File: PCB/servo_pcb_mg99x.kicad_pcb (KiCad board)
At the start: 2 copper layers, 35 x 16 mm, 42 parts, among them J1 power in, M1 M1, M2 M2, U1 MM32G0001, U2 SL7533-3, U3 BDR6121H, U4 INA180A2, U5 AS5600

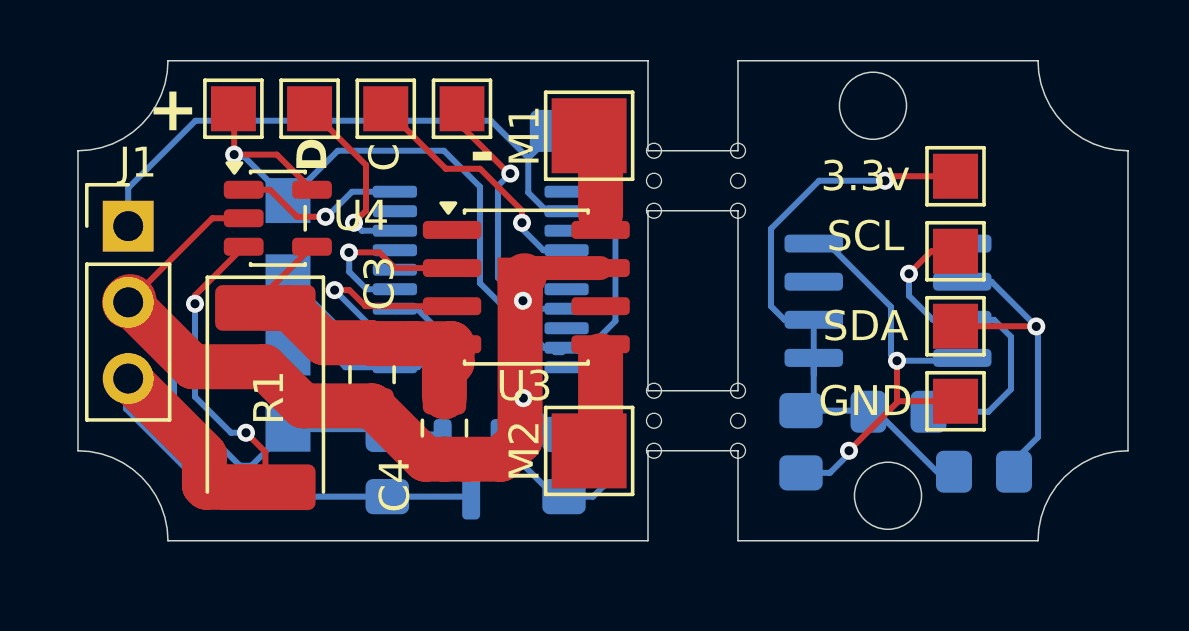
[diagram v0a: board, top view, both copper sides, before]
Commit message: updated pcb:added ground pours
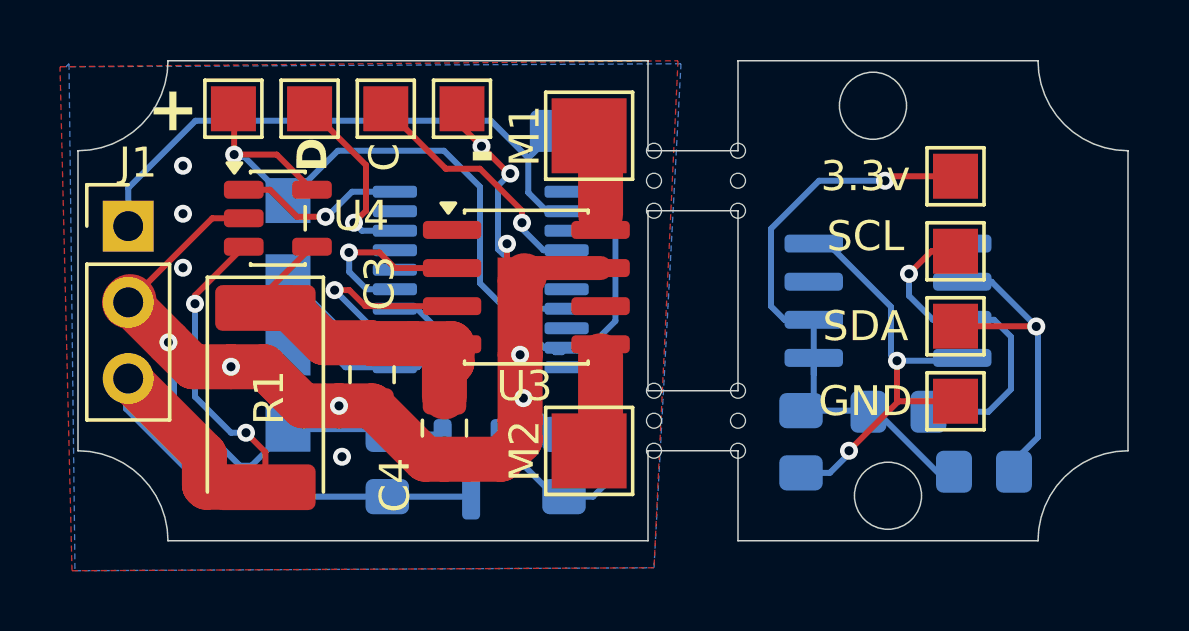
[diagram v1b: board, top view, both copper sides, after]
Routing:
- net GND: track 55.8 -> 56.4 mm, vias 3 -> 12
- added copper zone on B.Cu, net GND
- added copper zone on F.Cu, net GND
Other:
- board text added: "μDrive_1.0"
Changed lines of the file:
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@@
 		)
 		(fp_text user "${REFERENCE}"
-			(at 8.2 -14.17175 90)
+			(at 0 -0.1 90)
 			(layer "B.Fab")
 			(effects
@@
 		)
 		(property "Value" "10K"
-			(at 11 -3.65 0)
+			(at 0 -0.1 0)
 			(layer "B.Fab")
 			(effects
@@
 	)
 	(gr_text ".\n"
-		(at 58.694 42.504 0)
+		(at 69.7 40.9 0)
 		(layer "B.SilkS")
 		(effects
@@
 		)
 	)
+	(gr_text "μDrive_1.0\n"
+		(at 75.5 33.6 0)
+		(layer "B.SilkS")
+		(effects
+			(font
+				(size 1.5 1.5)
+				(thickness 0.2)
+			)
+			(justify left bottom mirror)
+		)
+	)
 	(segment
 		(start 73.34 44.0815)
@@
 	)
 	(segment
-		(start 75.231515 38.799485)
-		(end 75.497752 38.533248)
-		(width 0.8)
-		(layer "F.Cu")
-		(net 2)
-	)
-	(segment
-		(start 75.497752 38.533248)
-		(end 75.497752 38.179752)
-		(width 0.8)
+		(start 74.7 37.382)
+		(end 75.282 37.964)
+		(width 0.2)
 		(layer "F.Cu")
 		(net 2)
@@
 	(segment
 		(start 75.137 42.79)
-		(end 75.137 38.109)
+		(end 75.137 40.6)
 		(width 1.5)
 		(layer "F.Cu")
@@
 	)
 	(segment
+		(start 73.85 33.65)
+		(end 74.8 34.6)
+		(width 0.2)
+		(layer "F.Cu")
+		(net 2)
+	)
+	(segment
 		(start 62.074 38.853)
 		(end 62.080999 38.853)
@@
 	(segment
 		(start 67.9035 42.3035)
-		(end 70.202 42.3035)
+		(end 69.1 42.3035)
 		(width 1.5)
 		(layer "F.Cu")
@@
 	(segment
 		(start 64.227999 41)
-		(end 66.6 41)
+		(end 65.5 41)
 		(width 1.5)
 		(layer "F.Cu")
@@
 	)
 	(segment
-		(start 75.497752 38.179752)
-		(end 75.282 37.964)
-		(width 0.8)
+		(start 63.413999 40.186001)
+		(end 64.227999 41)
+		(width 1.5)
+		(layer "F.Cu")
+		(net 2)
+	)
+	(segment
+		(start 69.1 42.3035)
+		(end 70.202 42.3035)
+		(width 1.5)
 		(layer "F.Cu")
 		(net 2)
@@
 	(segment
 		(start 73.2 33)
-		(end 74.8 34.6)
+		(end 73.85 33.65)
 		(width 0.2)
 		(layer "F.Cu")
@@
 	)
 	(segment
+		(start 75.137 40.6)
+		(end 75.137 38.109)
+		(width 1.5)
+		(layer "F.Cu")
+		(net 2)
+	)
+	(segment
+		(start 74.7 36.9)
+		(end 74.7 37.382)
+		(width 0.2)
+		(layer "F.Cu")
+		(net 2)
+	)
+	(segment
 		(start 62.080999 38.853)
-		(end 64.227999 41)
+		(end 63.413999 40.186001)
 		(width 1.5)
 		(layer "F.Cu")
@@
 	)
 	(segment
+		(start 65.5 41)
+		(end 66.6 41)
+		(width 1.5)
+		(layer "F.Cu")
+		(net 2)
+	)
+	(segment
 		(start 74.8 34.6)
 		(end 74.809 34.591)
@@
 	)
 	(via
-		(at 75.231515 38.799485)
+		(at 69.2 44)
+		(size 0.6)
+		(drill 0.3)
+		(layers "F.Cu" "B.Cu")
+		(free yes)
+		(net 2)
+	)
+	(via
+		(at 69.1 42.3035)
+		(size 0.6)
+		(drill 0.3)
+		(layers "F.Cu" "B.Cu")
+		(net 2)
+	)
+	(via
+		(at 63.9 34.3)
+		(size 0.6)
+		(drill 0.3)
+		(layers "F.Cu" "B.Cu")
+		(free yes)
+		(net 2)
+	)
+	(via
+		(at 63.9 37.7)
 		(size 0.6)
 		(drill 0.3)
 		(layers "F.Cu" "B.Cu")
+		(free yes)
 		(net 2)
 	)
@@
 	)
 	(via
+		(at 65.5 41)
+		(size 0.6)
+		(drill 0.3)
+		(layers "F.Cu" "B.Cu")
+		(net 2)
+	)
+	(via
+		(at 74.7 36.9)
+		(size 0.6)
+		(drill 0.3)
+		(layers "F.Cu" "B.Cu")
+		(net 2)
+	)
+	(via
 		(at 75.245722 42.045722)
 		(size 0.6)
@@
 		(net 2)
 	)
+	(via
+		(at 73.85 33.65)
+		(size 0.6)
+		(drill 0.3)
+		(layers "F.Cu" "B.Cu")
+		(net 2)
+	)
+	(via
+		(at 75.137 40.6)
+		(size 0.6)
+		(drill 0.3)
+		(layers "F.Cu" "B.Cu")
+		(net 2)
+	)
+	(via
+		(at 63.9 35.9)
+		(size 0.6)
+		(drill 0.3)
+		(layers "F.Cu" "B.Cu")
+		(free yes)
+		(net 2)
+	)
+	(via
+		(at 63.413999 40.186001)
+		(size 0.6)
+		(drill 0.3)
+		(layers "F.Cu" "B.Cu")
+		(net 2)
+	)
 	(segment
 		(start 75.245722 42.045722)
@@
 	)
 	(segment
-		(start 75.231515 38.799485)
-		(end 75.49803 39.066)
+		(start 74.4 37.082)
+		(end 74.518 37.082)
 		(width 0.2)
 		(layer "B.Cu")
@@
 	)
 	(segment
-		(start 74.4 38.032)
-		(end 74.4 34.969472)
+		(start 63.6 42.1)
+		(end 63.6 40.379)
 		(width 0.2)
 		(layer "B.Cu")
@@
 	)
 	(segment
-		(start 63.6 42.1)
-		(end 63.6 40.379)
+		(start 75.282 37.964)
+		(end 74.4 37.082)
 		(width 0.2)
 		(layer "B.Cu")
@@
 	)
 	(segment
+		(start 75.282 37.964)
+		(end 75.282 38.84997)
+		(width 0.2)
+		(layer "B.Cu")
+		(net 2)
+	)
+	(segment
 		(start 72.327 43.255)
 		(end 72.554 43.482)
@@
 	)
 	(segment
-		(start 67.4 43.08)
-		(end 66.18 44.3)
+		(start 75.282 38.84997)
+		(end 75.49803 39.066)
 		(width 0.2)
 		(layer "B.Cu")
@@
 	)
 	(segment
-		(start 75.167485 38.799485)
-		(end 74.4 38.032)
+		(start 67.4 43.08)
+		(end 66.18 44.3)
 		(width 0.2)
 		(layer "B.Cu")
@@
 	)
 	(segment
-		(start 76.455 43.255)
-		(end 76.6 43.255)
+		(start 74.4 37.082)
+		(end 74.4 34.969472)
 		(width 0.2)
 		(layer "B.Cu")
@@
 	)
 	(segment
-		(start 70.535 43.08)
-		(end 70.71 43.255)
+		(start 74.4 34.969472)
+		(end 74.809 34.560472)
 		(width 0.2)
 		(layer "B.Cu")
@@
 	)
 	(segment
-		(start 75.231515 38.799485)
-		(end 75.167485 38.799485)
+		(start 76.455 43.255)
+		(end 76.6 43.255)
 		(width 0.2)
 		(layer "B.Cu")
@@
 	)
 	(segment
-		(start 74.4 34.969472)
-		(end 74.809 34.560472)
+		(start 70.535 43.08)
+		(end 70.71 43.255)
 		(width 0.2)
 		(layer "B.Cu")
@@
 	)
 	(segment
+		(start 74.518 37.082)
+		(end 74.7 36.9)
+		(width 0.2)
+		(layer "B.Cu")
+		(net 2)
+	)
+	(segment
 		(start 65.605044 32.425044)
 		(end 65.58 32.4)
@@
 		(net 30)
 	)
+	(zone
+		(net 2)
+		(net_name "GND")
+		(layer "F.Cu")
+		(hatch edge 0.5)
+		(connect_pads
+			(clearance 0.5)
+		)
+		(min_thickness 0.25)
+		(filled_areas_thickness no)
+		(fill yes
+			(thermal_gap 0.5)
+			(thermal_bridge_width 0.5)
+		)
+		(polygon
+			(pts
+				(xy 59.8 31) (xy 80.4 30.8) (xy 79.6 47.7) (xy 60.2 47.8)
+			)
+		)
+	)
+	(zone
+		(net 2)
+		(net_name "GND")
+		(layer "B.Cu")
+		(hatch edge 0.5)
+		(priority 1)
+		(connect_pads
+			(clearance 0.5)
+		)
+		(min_thickness 0.25)
+		(filled_areas_thickness no)
+		(fill yes
+			(thermal_gap 0.5)
+			(thermal_bridge_width 0.5)
+		)
+		(polygon
+			(pts
+				(xy 60.1 30.9) (xy 60.3 47.8) (xy 79.6 47.7) (xy 80.5 30.9) (xy 60 31)
+			)
+		)
+	)
 	(group ""

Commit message: updated  the pcb for generic motors
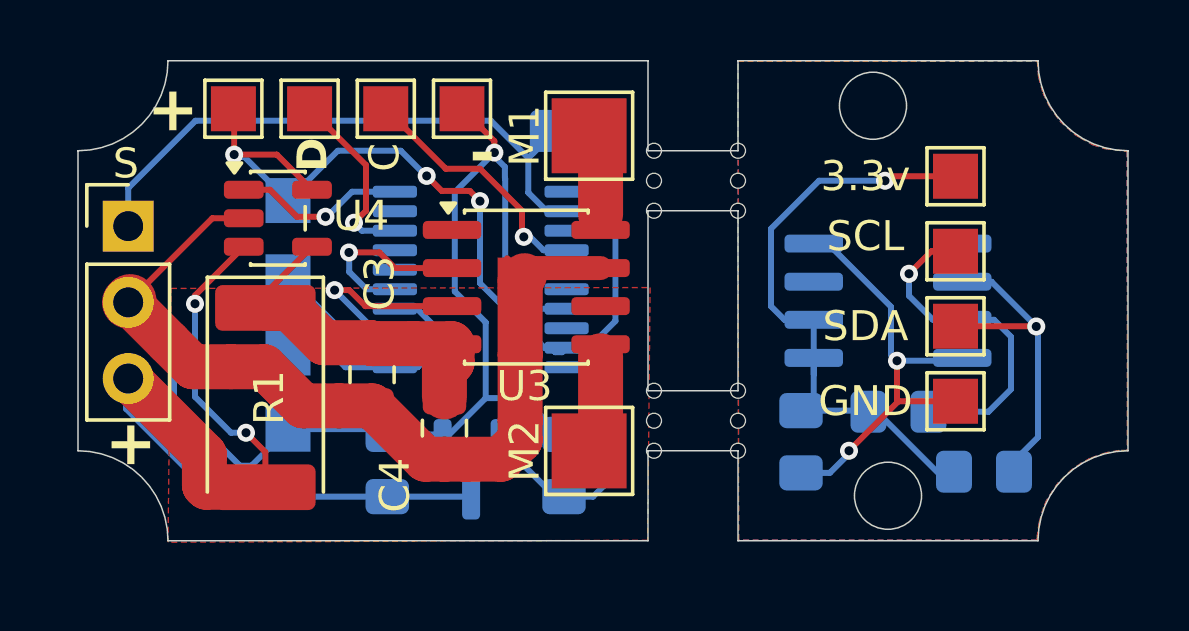
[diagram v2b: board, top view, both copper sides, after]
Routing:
- net GND: track 56.4 -> 68.1 mm, vias 12 -> 1
- net +3.3V: track 40.8 -> 40.5 mm, vias 1 -> 3
- added copper zone on B.Cu, net (none)
- added copper zone on F.Cu, net (none)
- removed copper zone on B.Cu, net GND
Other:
- board text added: "S"

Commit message: fix:update pcb footprint error ,cleanup micropython code
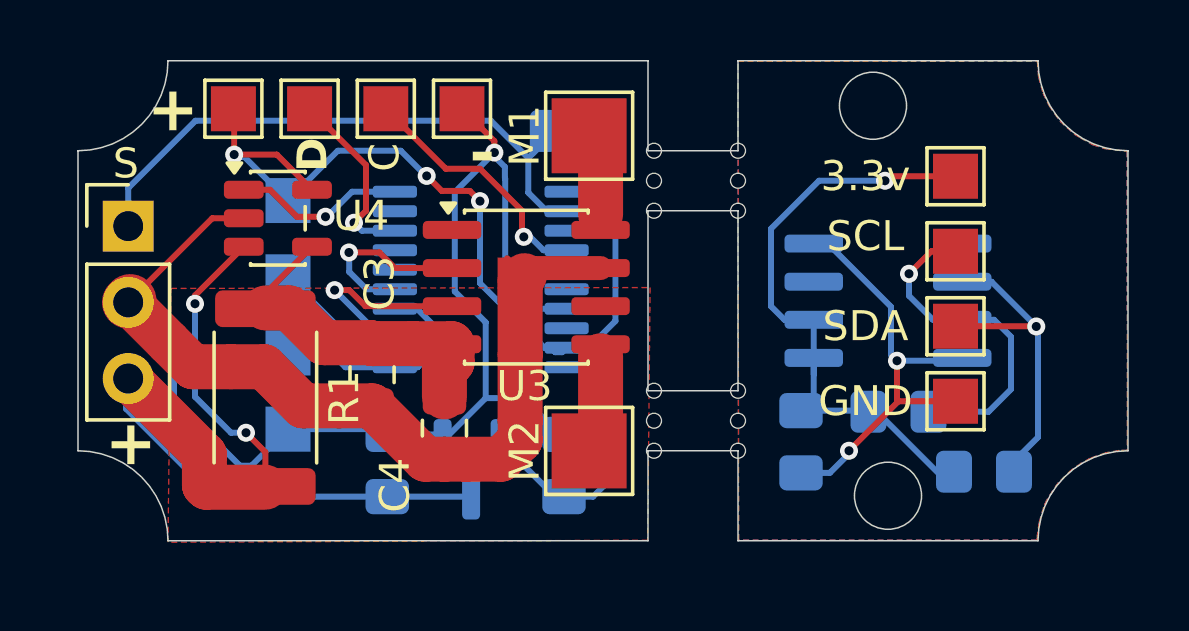
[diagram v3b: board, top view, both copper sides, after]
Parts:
- R1: footprint Diode_SMD:D_2512_6332Metric_Pad1.52x3.35mm_HandSolder -> Resistor_SMD:R_2512_6332Metric
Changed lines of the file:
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@@
 		(embedded_fonts no)
 	)
-	(footprint "Diode_SMD:D_2512_6332Metric_Pad1.52x3.35mm_HandSolder"
+	(footprint "Resistor_SMD:R_2512_6332Metric"
 		(layer "F.Cu")
 		(at 66.646 42.028 -90)
-		(descr "Diode SMD 2512 (6332 Metric), square (rectangular) end terminal, IPC-7351 nominal, (Body size source: http://www.tortai-tech.com/upload/download/2011102023233369053.pdf), generated with kicad-footprint-generator")
-		(tags "diode handsolder")
+		(descr "Resistor SMD 2512 (6332 Metric), square (rectangular) end terminal, IPC-7351 nominal, (Body size source: IPC-SM-782 page 72, https://www.pcb-3d.com/wordpress/wp-content/uploads/ipc-sm-782a_amendment_1_and_2.pdf), generated with kicad-footprint-generator")
+		(tags "resistor")
 		(property "Reference" "R1"
-			(at 0 -0.127 90)
+			(at 0 -2.63 270)
 			(layer "F.SilkS")
 			(effects
@@
 		)
 		(property "Value" "0.01R"
-			(at 0.508 -0.127 90)
+			(at 0 2.63 270)
 			(layer "F.Fab")
 			(effects
@@
 			)
 		)
-		(property "Datasheet" "~"
-			(at 0 0 90)
+		(property "Datasheet" ""
+			(at 0 0 270)
 			(layer "F.Fab")
 			(hide yes)
@@
 			)
 		)
-		(property "Description" "Resistor"
-			(at 0 0 90)
+		(property "Description" ""
+			(at 0 0 270)
 			(layer "F.Fab")
 			(hide yes)
@@
 		(attr smd)
 		(fp_line
-			(start -4.01 1.935)
-			(end 3.15 1.935)
+			(start -2.177064 1.71)
+			(end 2.177064 1.71)
 			(stroke
 				(width 0.12)
@@
 		)
 		(fp_line
-			(start -4.01 -1.935)
-			(end -4.01 1.935)
+			(start -2.177064 -1.71)
+			(end 2.177064 -1.71)
 			(stroke
 				(width 0.12)
@@
 		)
 		(fp_line
-			(start 3.15 -1.935)
-			(end -4.01 -1.935)
-			(stroke
-				(width 0.12)
-				(type solid)
-			)
-			(layer "F.SilkS")
-		)
-		(fp_line
-			(start -4 1.93)
-			(end -4 -1.93)
+			(start -3.83 1.93)
+			(end -3.83 -1.93)
 			(stroke
 				(width 0.05)
@@
 		)
 		(fp_line
-			(start 4 1.93)
-			(end -4 1.93)
+			(start 3.83 1.93)
+			(end -3.83 1.93)
 			(stroke
 				(width 0.05)
@@
 		)
 		(fp_line
-			(start -4 -1.93)
-			(end 4 -1.93)
+			(start -3.83 -1.93)
+			(end 3.83 -1.93)
 			(stroke
 				(width 0.05)
@@
 		)
 		(fp_line
-			(start 4 -1.93)
-			(end 4 1.93)
+			(start 3.83 -1.93)
+			(end 3.83 1.93)
 			(stroke
 				(width 0.05)
@@
 		(fp_line
 			(start -3.15 1.6)
-			(end 3.15 1.6)
+			(end -3.15 -1.6)
 			(stroke
 				(width 0.1)
@@
 		(fp_line
 			(start 3.15 1.6)
+			(end -3.15 1.6)
+			(stroke
+				(width 0.1)
+				(type solid)
+			)
+			(layer "F.Fab")
+		)
+		(fp_line
+			(start -3.15 -1.6)
 			(end 3.15 -1.6)
 			(stroke
@@
 		)
 		(fp_line
-			(start -3.15 -0.8)
-			(end -3.15 1.6)
-			(stroke
-				(width 0.1)
-				(type solid)
-			)
-			(layer "F.Fab")
-		)
-		(fp_line
-			(start -2.35 -1.6)
-			(end -3.15 -0.8)
-			(stroke
-				(width 0.1)
-				(type solid)
-			)
-			(layer "F.Fab")
-		)
-		(fp_line
 			(start 3.15 -1.6)
-			(end -2.35 -1.6)
+			(end 3.15 1.6)
 			(stroke
 				(width 0.1)
@@
 		)
 		(fp_text user "${REFERENCE}"
-			(at -0.254 0.762 90)
+			(at 0 0 270)
 			(layer "F.Fab")
 			(effects
@@
 		)
 		(pad "1" smd roundrect
-			(at -2.9875 0 270)
-			(size 1.525 3.35)
+			(at -2.9625 0 270)
+			(size 1.225 3.35)
 			(layers "F.Cu" "F.Mask" "F.Paste")
-			(roundrect_rratio 0.163934)
+			(roundrect_rratio 0.204082)
 			(net 5 "/DRIVER VCC")
 			(pintype "passive")
 		)
 		(pad "2" smd roundrect
-			(at 2.9875 0 270)
-			(size 1.525 3.35)
+			(at 2.9625 0 270)
+			(size 1.225 3.35)
 			(layers "F.Cu" "F.Mask" "F.Paste")
-			(roundrect_rratio 0.163934)
+			(roundrect_rratio 0.204082)
 			(net 4 "VCC")
 			(pintype "passive")
 		)
 		(embedded_fonts no)
-		(model "${KICAD9_3DMODEL_DIR}/Diode_SMD.3dshapes/D_2512_6332Metric.step"
+		(model "${KICAD9_3DMODEL_DIR}/Resistor_SMD.3dshapes/R_2512_6332Metric.step"
 			(offset
 				(xyz 0 0 0)
